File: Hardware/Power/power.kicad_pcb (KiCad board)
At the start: 4 copper layers, 70 x 67.5 mm, 33 parts, among them J1 Conn_02x23_Odd_Even, J2 Screw_Terminal_01x03, J3 Conn_02x23_Odd_Even, Q1 SI2347DS-T1-GE3, T1 10V, T2 VCC, T3 GND, T4 GND, T5 5V, T6 3V3, T7 GND, U1 TPS563200, U2 TPS563300DRLR, U3 LM1117-3.3

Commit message: schematic update & pcb update
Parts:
- removed C17: 22u, Capacitor_SMD:C_0603_1608Metric_Pad1.08x0.95mm_HandSolder
- removed D5: LD3V3, LED_SMD:LED_0603_1608Metric_Pad1.05x0.95mm_HandSolder
- removed J2: Screw_Terminal_01x03, PLC_STM_Power:TBC05031GG
- removed R8, R9: 1k, Resistor_SMD:R_0603_1608Metric_Pad0.98x0.95mm_HandSolder
- removed U3: LM1117-3.3, Package_TO_SOT_SMD:SOT-223-3_TabPin2
- added C1: 10u, Capacitor_SMD:C_0603_1608Metric_Pad1.08x0.95mm_HandSolder, F.Cu at (138.3, 72.5)
- added C10: 10u, Capacitor_SMD:C_0603_1608Metric_Pad1.08x0.95mm_HandSolder, F.Cu at (142.7, 72.5)
- added C11: 10u, Capacitor_SMD:C_0603_1608Metric_Pad1.08x0.95mm_HandSolder, F.Cu at (142.7, 75.0)
- added C14: 100n, Capacitor_SMD:C_0603_1608Metric_Pad1.08x0.95mm_HandSolder, F.Cu at (142.7, 82.5)
- added C2: 10u, Capacitor_SMD:C_0603_1608Metric_Pad1.08x0.95mm_HandSolder, F.Cu at (138.3, 75.0)
- added C5: 100n, Capacitor_SMD:C_0603_1608Metric_Pad1.08x0.95mm_HandSolder, F.Cu at (138.3, 80.0)
- added C8: 22u, Capacitor_SMD:C_0603_1608Metric_Pad1.08x0.95mm_HandSolder, F.Cu at (138.3, 85.0)
- added C9: 22u, Capacitor_SMD:C_0603_1608Metric_Pad1.08x0.95mm_HandSolder, F.Cu at (138.3, 87.5)
- added F2: 6V/1A, Fuse:Fuse_0805_2012Metric_Pad1.15x1.40mm_HandSolder, F.Cu at (168.3, 84.4)
- added J1: POWER, PLC_STM:1725656, F.Cu at (139.2, 100.1)
- added L1: 3u3/4A95, Inductor_SMD:L_TDK_VLS6045EX_VLS6045AF, F.Cu at (166.9, 75.0)
- added PS1: DPUN02N-15, PLC_STM:DPUN02N15, F.Cu at (141.3, 64.4)
- added R2: 56k2, Resistor_SMD:R_0603_1608Metric_Pad0.98x0.95mm_HandSolder, F.Cu at (147.1, 72.5)
- added R20: 10k, Resistor_SMD:R_0603_1608Metric_Pad0.98x0.95mm_HandSolder, F.Cu at (147.1, 80.0)
- added R4: 1k, Resistor_SMD:R_0603_1608Metric_Pad0.98x0.95mm_HandSolder, F.Cu at (147.1, 75.0)
- added T10: GND, TestPoint:TestPoint_Pad_1.0x1.0mm, F.Cu at (153.8, 85.0)
- added T8: 5V, TestPoint:TestPoint_Pad_1.0x1.0mm, F.Cu at (153.8, 78.8)
- added T9: 3V3, TestPoint:TestPoint_Pad_1.0x1.0mm, F.Cu at (153.8, 81.9)
- C15: value 100n -> 22u
- D3: value LD10V -> LD5V
- D4: value LD10V -> LD3V3
- T1: value 10V -> VCC
- T2: value VCC -> 15V
- T4: value GND -> 5V
- T5: value 5V -> GND
- T6: value 3V3 -> +15V
- T7: value GND -> -15V
- U2: value TPS563300DRLR -> LM1117-3.3; footprint Package_TO_SOT_SMD:SOT-583-8 -> Package_TO_SOT_SMD:SOT-223-3_TabPin2
- moved Q1 84.7 mm to (138.8, 91.0)
- moved D3 74.9 mm to (151.4, 87.8)
- moved D4 74.9 mm to (151.4, 90.4)
- moved U1 74.4 mm to (143.9, 91.2)
- moved U2 72.2 mm to (165.2, 65.1)
- moved C4 67.6 mm to (138.3, 77.5)
- moved C7 67.4 mm to (138.3, 82.5)
- moved D2 65.4 mm to (157.9, 91.4)
- moved C12 63.8 mm to (142.7, 77.5)
- moved C13 63.8 mm to (142.7, 80.0)
- moved R1 63.8 mm to (142.7, 87.5)
- moved T6 63.6 mm to (153.8, 72.8)
- moved T7 63.6 mm to (153.8, 75.8)
- moved C15 63.5 mm to (142.7, 85.0)
- moved R5 62.8 mm to (147.1, 77.5)
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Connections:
- D4 pad 2: /power_section/D10V_R1k -> /power_section/D3V3_R1k
- R5 pad 1: Net-(C8-Pad1) -> /power_section/VO_+3.3V
- R5 pad 2: /power_section/D5V_R1k -> /power_section/D3V3_R1k
- T1 pad 1: +10V -> /power_section/RPP_D
- T2 pad 1: /power_section/RPP_D -> +15V
- T4 pad 1: GND -> Net-(C8-Pad1)
- T5 pad 1: +5V -> GND
- T6 pad 1: /power_section/VO_+3.3V -> +15V
- T7 pad 1: GND -> -15V
- U1 pad 3: +10V -> +15V
- U1 pad 5: Net-(U1-EN) -> +15V
- U2 pad 1: unconnected-(U2-NC-Pad1) -> GND
- U2 pad 2: unconnected-(U2-EN-Pad2) -> /power_section/VO_+3.3V
- U2 pad 3: /power_section/VCC_IN -> +5V

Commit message: schematic update & pcb update
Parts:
- removed the J1 at (119.2, 52.5)
- added J2: NUCLEO LEFT, PLC_STM:PRT12790, F.Cu at (119.2, 52.5)
- J3: value Conn_02x23_Odd_Even -> NUCLEO RIGHT; footprint PLC_STM_Power:PRT12790 -> PLC_STM:PRT12790
- moved J3 56.0 mm to (180.2, 52.5), turned to -90 degrees
- moved F3 40.4 mm to (137.5, 61.2), turned to 90 degrees
- moved PS1 40.3 mm to (142.7, 104.8)
- moved D1 36.1 mm to (131.8, 92.0), turned to 90 degrees
- moved C1 34.7 mm to (171.8, 81.8), turned to 90 degrees
- moved C2 32.1 mm to (169.8, 81.8), turned to 90 degrees
- moved C10 32.0 mm to (158.6, 100.2), turned to 180 degrees
- moved F1 31.8 mm to (131.8, 99.8), turned to -90 degrees
- moved T1 30.1 mm to (128.5, 93.0), turned to -90 degrees
- moved C11 27.3 mm to (152.6, 100.4)
- moved C8 26.6 mm to (163.5, 76.3), turned to 90 degrees
- moved C9 25.9 mm to (161.8, 76.3), turned to 90 degrees
- moved C5 25.7 mm to (164.0, 81.8), turned to 90 degrees
- moved D4 25.3 mm to (136.8, 69.8), turned to 180 degrees
- moved U1 24.7 mm to (166.8, 81.8), turned to 90 degrees
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- renumbered R20 to R3
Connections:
- net Net-(C8-Pad1) renamed /power_section/+5V_OUT
- net Net-(U1-SW) renamed /power_section/SW_+5V
- net Net-(U1-VBST) renamed /power_section/VBST_+5V
- net Net-(U1-VFB) renamed /power_section/FB_+5V
- F2 pad 2: +3V3 -> +5V
- J3 pad 1: unconnected-(J3-Pin_1-Pad1) -> UART6_TX
- J3 pad 10: unconnected-(J3-Pin_10-Pad10) -> AO_1
- J3 pad 11: unconnected-(J3-Pin_11-Pad11) -> UART6_TX
- J3 pad 12: unconnected-(J3-Pin_12-Pad12) -> ANALOG_IN6
- J3 pad 13: unconnected-(J3-Pin_13-Pad13) -> CAN2_RX
- J3 pad 14: unconnected-(J3-Pin_14-Pad14) -> ANALOG_IN7
- J3 pad 17: unconnected-(J3-Pin_17-Pad17) -> AO_0
- J3 pad 2: unconnected-(J3-Pin_2-Pad2) -> CAN1_RX
- J3 pad 21: unconnected-(J3-Pin_21-Pad21) -> +15V
- J3 pad 23: unconnected-(J3-Pin_23-Pad23) -> AVDD
- J3 pad 25: unconnected-(J3-Pin_25-Pad25) -> AGND
- J3 pad 27: unconnected-(J3-Pin_27-Pad27) -> GND
- J3 pad 39: unconnected-(J3-Pin_39-Pad39) -> GND
- J3 pad 4: unconnected-(J3-Pin_4-Pad4) -> CAN1_TX
- J3 pad 40: unconnected-(J3-Pin_40-Pad40) -> UART6_TX
- J3 pad 42: unconnected-(J3-Pin_42-Pad42) -> UART6_RX
- J3 pad 44: unconnected-(J3-Pin_44-Pad44) -> UART5_TX
- J3 pad 46: unconnected-(J3-Pin_46-Pad46) -> UART5_RX
- J3 pad 5: unconnected-(J3-Pin_5-Pad5) -> CAN2_TX
- J3 pad 6: unconnected-(J3-Pin_6-Pad6) -> AVDD
- J3 pad 7: unconnected-(J3-Pin_7-Pad7) -> CAN2_RX
- J3 pad 8: unconnected-(J3-Pin_8-Pad8) -> GND
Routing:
- net +15V: track 0.00 -> 75.1 mm
- net +5V: track 0.00 -> 69.8 mm
- net -15V: track 0.00 -> 62.0 mm
- net GND: track 0.00 -> 32.2 mm, vias 0 -> 24
- net /power_section/VCC_IN: track 0.00 -> 22.4 mm
- net +3V3: track 0.00 -> 19.3 mm
- net /power_section/+5V_OUT: track 0.00 -> 8.00 mm
- net +24V: track 0.00 -> 7.11 mm
- net /power_section/VO_+3.3V: track 0.00 -> 5.12 mm
- net /power_section/FB_+5V: track 0.00 -> 4.28 mm
- net /power_section/VBST_+5V: track 0.00 -> 4.07 mm
- net /power_section/D5V_R1k: track 0.00 -> 3.24 mm
- net /power_section/RPP_D: track 0.00 -> 2.62 mm
- net /power_section/D3V3_R1k: track 0.00 -> 1.77 mm
- added copper zone on F.Cu, net +5V
- added copper zone on F.Cu, net /power_section/+5V_OUT
- added copper zone on F.Cu, net /power_section/RPP_D
- added copper zone on F.Cu, net /power_section/RPP_G
- added copper zone on F.Cu, net /power_section/SW_+5V
- added copper zone on F.Cu, net /power_section/VCC_IN
- added copper zone on F.Cu, net /power_section/VO_+3.3V
- added copper zone on B.Cu, net GND
- added copper zone on F.Cu, net GND
- added copper zone on In1.Cu, net GND
- added copper zone on In2.Cu, net GND

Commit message: digital output & power finished
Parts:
- renumbered C12 to C10, C13 to C11, C10 to C12, C11 to C13, T8 to T6, T6 to T7, T7 to T8
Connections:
- C3 pad 1: /power_section/VCC_IN -> +24V
- C4 pad 1: /power_section/VCC_IN -> +24V
- C6 pad 1: /power_section/VCC_IN -> +24V
- C7 pad 1: /power_section/VCC_IN -> +24V
- D2 pad 1: /power_section/VCC_IN -> +24V
- F1 pad 2: +24V -> VCC
- J1 pad 2: +24V -> VCC
- J2 pad 10: UART5_TX -> +15V
- J2 pad 11: GND -> unconnected-(J2-Pin_11-Pad11)
- J2 pad 12: UART5_RX -> unconnected-(J2-Pin_12-Pad12)
- J2 pad 13: GND -> unconnected-(J2-Pin_13-Pad13)
- J2 pad 15: +5V -> unconnected-(J2-Pin_15-Pad15)
- J2 pad 18: -15V -> unconnected-(J2-Pin_18-Pad18)
- J2 pad 19: unconnected-(J2-Pin_19-Pad19) -> GND
- J2 pad 20: unconnected-(J2-Pin_20-Pad20) -> GND
- J2 pad 22: UART2_RX -> GND
- J2 pad 24: UART2_TX -> unconnected-(J2-Pin_24-Pad24)
- J2 pad 25: unconnected-(J2-Pin_25-Pad25) -> +3V3
- J2 pad 26: unconnected-(J2-Pin_26-Pad26) -> -15V
- J2 pad 27: unconnected-(J2-Pin_27-Pad27) -> +5V
- J2 pad 29: unconnected-(J2-Pin_29-Pad29) -> +24V
- J2 pad 30: GND -> unconnected-(J2-Pin_30-Pad30)
- J2 pad 39: GND -> unconnected-(J2-Pin_39-Pad39)
- J2 pad 41: CAN1_RX -> unconnected-(J2-Pin_41-Pad41)
- J2 pad 43: CAN1_TX -> unconnected-(J2-Pin_43-Pad43)
- J2 pad 6: UART4_TX -> unconnected-(J2-Pin_6-Pad6)
- J2 pad 7: +3V3 -> unconnected-(J2-Pin_7-Pad7)
- J2 pad 8: UART4_RX -> unconnected-(J2-Pin_8-Pad8)
- J2 pad 9: +5V -> unconnected-(J2-Pin_9-Pad9)
- J3 pad 1: UART6_TX -> unconnected-(J3-Pin_1-Pad1)
- J3 pad 10: AO_1 -> unconnected-(J3-Pin_10-Pad10)
- J3 pad 11: UART6_TX -> unconnected-(J3-Pin_11-Pad11)
- J3 pad 12: ANALOG_IN6 -> unconnected-(J3-Pin_12-Pad12)
- J3 pad 13: CAN2_RX -> unconnected-(J3-Pin_13-Pad13)
- J3 pad 14: ANALOG_IN7 -> unconnected-(J3-Pin_14-Pad14)
- J3 pad 17: AO_0 -> unconnected-(J3-Pin_17-Pad17)
- J3 pad 2: CAN1_RX -> unconnected-(J3-Pin_2-Pad2)
- J3 pad 20: unconnected-(J3-Pin_20-Pad20) -> GND
- J3 pad 21: +15V -> unconnected-(J3-Pin_21-Pad21)
- J3 pad 23: AVDD -> unconnected-(J3-Pin_23-Pad23)
- J3 pad 25: AGND -> unconnected-(J3-Pin_25-Pad25)
- J3 pad 27: GND -> unconnected-(J3-Pin_27-Pad27)
- J3 pad 4: CAN1_TX -> unconnected-(J3-Pin_4-Pad4)
- J3 pad 40: UART6_TX -> unconnected-(J3-Pin_40-Pad40)
- J3 pad 42: UART6_RX -> unconnected-(J3-Pin_42-Pad42)
- J3 pad 44: UART5_TX -> unconnected-(J3-Pin_44-Pad44)
- J3 pad 46: UART5_RX -> unconnected-(J3-Pin_46-Pad46)
- J3 pad 5: CAN2_TX -> unconnected-(J3-Pin_5-Pad5)
- J3 pad 6: AVDD -> unconnected-(J3-Pin_6-Pad6)
- J3 pad 7: CAN2_RX -> unconnected-(J3-Pin_7-Pad7)
- J3 pad 8: GND -> unconnected-(J3-Pin_8-Pad8)
- PS1 pad 1: /power_section/VCC_IN -> +24V
- Q1 pad 2: /power_section/VCC_IN -> +24V
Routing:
- net +24V: track 7.11 -> 67.0 mm, vias 0 -> 1
- net +15V: track 75.1 -> 112.8 mm, vias 0 -> 1
- net /power_section/VCC_IN: track 22.4 -> 0.00 mm
- net +3V3: track 19.3 -> 39.2 mm, vias 0 -> 1
- net +5V: track 69.8 -> 57.2 mm
- net VCC: track 0.00 -> 7.11 mm
- net -15V: track 62.0 -> 62.6 mm
- added copper zone on F.Cu, net +24V
- removed copper zone on F.Cu, net /power_section/VCC_IN
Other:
- board text removed: "®©®"

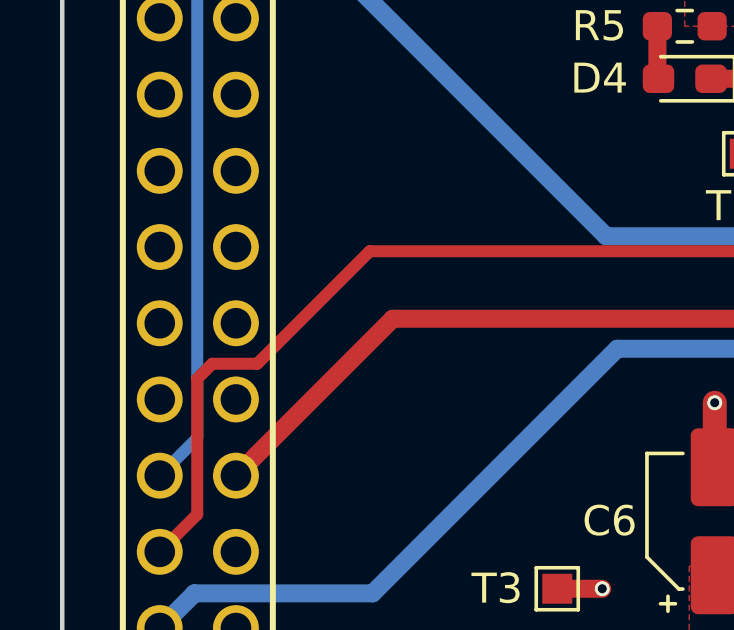
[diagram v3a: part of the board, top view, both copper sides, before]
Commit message: analog & can finished
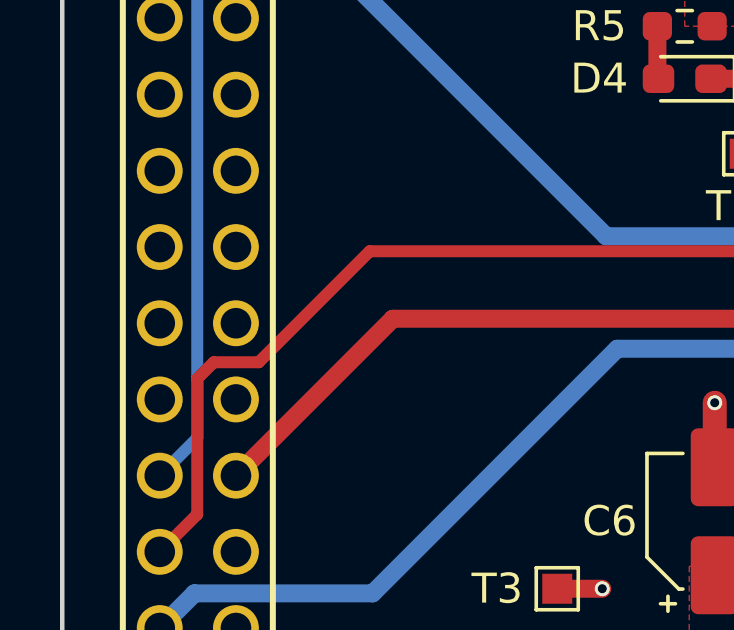
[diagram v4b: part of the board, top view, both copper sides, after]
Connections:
- J3 pad 39: GND -> unconnected-(J3-Pin_39-Pad39)
- J3 pad 9: unconnected-(J3-Pin_9-Pad9) -> GND
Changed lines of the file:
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@@
 	(net 26 "unconnected-(J3-Pin_15-Pad15)")
 	(net 27 "unconnected-(J3-Pin_29-Pad29)")
-	(net 28 "unconnected-(J3-Pin_9-Pad9)")
+	(net 28 "unconnected-(J3-Pin_39-Pad39)")
 	(net 29 "unconnected-(J3-Pin_41-Pad41)")
 	(net 30 "unconnected-(J3-Pin_19-Pad19)")
@@
 			(layers "*.Cu" "*.Mask")
 			(remove_unused_layers no)
-			(net 28 "unconnected-(J3-Pin_9-Pad9)")
+			(net 2 "GND")
 			(pinfunction "Pin_9")
-			(pintype "passive+no_connect")
+			(pintype "passive")
 		)
 		(pad "10" thru_hole circle
@@
 			(layers "*.Cu" "*.Mask")
 			(remove_unused_layers no)
-			(net 2 "GND")
+			(net 28 "unconnected-(J3-Pin_39-Pad39)")
 			(pinfunction "Pin_39")
-			(pintype "passive")
+			(pintype "passive+no_connect")
 		)
 		(pad "40" thru_hole circle
@@
 		(layer "Dwgs.User")
 		(pts
-			(xy 135 48.5) (xy 137 56.5)
-		)
-		(height 6)
-		(orientation 1)
-		(format
-			(prefix "")
-			(suffix "")
-			(units 3)
-			(units_format 1)
-			(precision 4)
-			(suppress_zeroes yes)
-		)
-		(style
-			(thickness 0.1)
-			(arrow_length 1.27)
-			(text_position_mode 1)
-			(arrow_direction outward)
-			(extension_height 0.58642)
-			(extension_offset 0.5)
-			(keep_text_aligned yes)
-		)
-		(gr_text "8 mm"
-			(at 141 52.5 90)
-			(layer "Dwgs.User")
-			(effects
-				(font
-					(size 0.8 0.8)
-					(thickness 0.1)
-				)
-			)
-		)
-	)
-	(dimension
-		(type orthogonal)
-		(layer "Dwgs.User")
-		(pts
 			(xy 116 112) (xy 186 112)
 		)
@@
 		)
 	)
-	(dimension
-		(type orthogonal)
-		(layer "Dwgs.User")
-		(pts
-			(xy 135 48.5) (xy 167 48.5)
-		)
-		(height -2.5)
-		(orientation 0)
-		(format
-			(prefix "")
-			(suffix "")
-			(units 3)
-			(units_format 1)
-			(precision 4)
-			(suppress_zeroes yes)
-		)
-		(style
-			(thickness 0.1)
-			(arrow_length 1.27)
-			(text_position_mode 1)
-			(arrow_direction outward)
-			(extension_height 0.58642)
-			(extension_offset 0.5)
-			(keep_text_aligned yes)
-		)
-		(gr_text "32 mm"
-			(at 151 46 0)
-			(layer "Dwgs.User")
-			(effects
-				(font
-					(size 0.8 0.8)
-					(thickness 0.1)
-				)
-			)
-		)
-	)
 	(segment
 		(start 133.25 109.71)
@@
 	)
 	(segment
-		(start 150.25 66.75)
-		(end 149.1375 65.6375)
-		(width 0.6)
+		(start 120.5 79.75)
+		(end 121.05 79.2)
+		(width 0.4)
 		(layer "F.Cu")
 		(net 3)
 	)
 	(segment
-		(start 119.25 85.52)
-		(end 120.5 84.27)
-		(width 0.4)
+		(start 150.25 66.75)
+		(end 149.1375 65.6375)
+		(width 0.6)
 		(layer "F.Cu")
 		(net 3)
 	)
 	(segment
-		(start 121 79.25)
-		(end 122.5 79.25)
+		(start 126.25 75.5)
+		(end 154.975 75.5)
 		(width 0.4)
 		(layer "F.Cu")
@@
 	)
 	(segment
-		(start 149.1375 65.6375)
-		(end 149.1375 64.25)
-		(width 0.6)
+		(start 120.5 84.27)
+		(end 120.5 79.75)
+		(width 0.4)
 		(layer "F.Cu")
 		(net 3)
 	)
 	(segment
-		(start 120.5 84.27)
-		(end 120.5 79.75)
-		(width 0.4)
+		(start 149.1375 65.6375)
+		(end 149.1375 64.25)
+		(width 0.6)
 		(layer "F.Cu")
 		(net 3)
 	)
 	(segment
-		(start 126.25 75.5)
-		(end 154.975 75.5)
+		(start 119.25 85.52)
+		(end 120.5 84.27)
 		(width 0.4)
 		(layer "F.Cu")
@@
 	)
 	(segment
-		(start 122.5 79.25)
+		(start 122.55 79.2)
 		(end 126.25 75.5)
 		(width 0.4)
@@
 	)
 	(segment
-		(start 120.5 79.75)
-		(end 121 79.25)
+		(start 121.05 79.2)
+		(end 122.55 79.2)
 		(width 0.4)
 		(layer "F.Cu")

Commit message: small adjustments and final revision
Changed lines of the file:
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@@
+		(layer "Dwgs.User")
+		(pts
+			(xy 118.02 51.105) (xy 184.02 51.105)
+		)
+		(height -5.105)
+		(orientation 0)
+		(format
+			(prefix "")
+			(suffix "")
+			(units 3)
+			(units_format 1)
+			(precision 4)
+			(suppress_zeroes yes)
+		)
+		(style
+			(thickness 0.1)
+			(arrow_length 1.27)
+			(text_position_mode 1)
+			(arrow_direction outward)
+			(extension_height 0.58642)
+			(extension_offset 0.5)
+			(keep_text_aligned yes)
+		)
+		(gr_text "66 mm"
+			(at 151.02 46 0)
+			(layer "Dwgs.User")
+			(effects
+				(font
+					(size 0.8 0.8)
+					(thickness 0.1)
+				)
+			)
+		)
+	)
+	(dimension
+		(type orthogonal)
 		(layer "Dwgs.User")
 		(pts
@@
 	)
 	(segment
-		(start 169.75 83.7)
-		(end 169.75 82.7125)
-		(width 0.6)
-		(layer "F.Cu")
-		(net 8)
-	)
-	(segment
 		(start 164.25 87.75)
 		(end 170.5 87.75)
@@
 	)
 	(segment
+		(start 159.4625 97.2625)
+		(end 159 96.8)
+		(width 0.6)
+		(layer "F.Cu")
+		(net 8)
+	)
+	(segment
 		(start 170.5 87.75)
 		(end 171.75 86.5)
@@
 	)
 	(segment
-		(start 158.2 96.8)
-		(end 159.5 95.5)
+		(start 159.4625 100.4)
+		(end 159.4625 97.2625)
 		(width 0.6)
 		(layer "F.Cu")
@@
 	)
 	(segment
-		(start 158.2 96.8)
-		(end 157.2 96.8)
-		(width 0.6)
-		(layer "F.Cu")
-		(net 8)
-	)
-	(segment
-		(start 168 84.45)
-		(end 169 84.45)
-		(width 0.6)
+		(start 169.75 83.85)
+		(end 169.75 82.7125)
+		(width 0.4)
 		(layer "F.Cu")
 		(net 8)
@@
 	)
 	(segment
-		(start 159.4625 98.0625)
-		(end 158.2 96.8)
-		(width 0.6)
-		(layer "F.Cu")
-		(net 8)
-	)
-	(segment
 		(start 161.8125 101.4125)
 		(end 160.65 100.25)
@@
 	)
 	(segment
+		(start 157.2 96.8)
+		(end 159 96.8)
+		(width 0.6)
+		(layer "F.Cu")
+		(net 8)
+	)
+	(segment
+		(start 167.7 84.1)
+		(end 168 84.4)
+		(width 0.4)
+		(layer "F.Cu")
+		(net 8)
+	)
+	(segment
+		(start 168 84.4)
+		(end 169.2 84.4)
+		(width 0.4)
+		(layer "F.Cu")
+		(net 8)
+	)
+	(segment
 		(start 171.75 86.5)
 		(end 171.75 82.7125)
@@
 	)
 	(segment
-		(start 167.7 84.15)
-		(end 168 84.45)
-		(width 0.6)
-		(layer "F.Cu")
-		(net 8)
-	)
-	(segment
-		(start 159.4625 100.4)
-		(end 159.4625 98.0625)
+		(start 167.7 82.9875)
+		(end 167.7 84.1)
+		(width 0.4)
+		(layer "F.Cu")
+		(net 8)
+	)
+	(segment
+		(start 159.5 96.3)
+		(end 159.5 92.5)
 		(width 0.6)
 		(layer "F.Cu")
@@
 	)
 	(segment
-		(start 167.7 82.9875)
-		(end 167.7 84.15)
-		(width 0.6)
-		(layer "F.Cu")
-		(net 8)
-	)
-	(segment
 		(start 161.8125 104.3875)
 		(end 161.8125 101.4125)
@@
 	)
 	(segment
+		(start 169.2 84.4)
+		(end 169.75 83.85)
+		(width 0.4)
+		(layer "F.Cu")
+		(net 8)
+	)
+	(segment
 		(start 174.25 82.7)
 		(end 171.7625 82.7)
@@
 	)
 	(segment
-		(start 159.5 95.5)
-		(end 159.5 92.5)
-		(width 0.6)
-		(layer "F.Cu")
-		(net 8)
-	)
-	(segment
 		(start 160.65 100.25)
 		(end 159.4625 100.25)
@@
 	)
 	(segment
-		(start 169 84.45)
-		(end 169.75 83.7)
+		(start 159 96.8)
+		(end 159.5 96.3)
 		(width 0.6)
 		(layer "F.Cu")
@@
 	)
 	(segment
-		(start 154 79.5)
-		(end 154 87)
-		(width 0.6)
-		(layer "B.Cu")
-		(net 8)
-	)
-	(segment
-		(start 121.79 62.66)
-		(end 134.13 75)
-		(width 0.6)
-		(layer "B.Cu")
-		(net 8)
-	)
-	(segment
-		(start 149.5 75)
-		(end 154 79.5)
-		(width 0.6)
-		(layer "B.Cu")
-		(net 8)
-	)
-	(segment
-		(start 154 87)
-		(end 158 91)
-		(width 0.6)
-		(layer "B.Cu")
-		(net 8)
-	)
-	(segment
-		(start 134.13 75)
-		(end 149.5 75)
+		(start 158 91)
+		(end 154.8 87.8)
+		(width 0.6)
+		(layer "B.Cu")
+		(net 8)
+	)
+	(segment
+		(start 148.6 74)
+		(end 133.13 74)
+		(width 0.6)
+		(layer "B.Cu")
+		(net 8)
+	)
+	(segment
+		(start 154.8 80.2)
+		(end 148.6 74)
+		(width 0.6)
+		(layer "B.Cu")
+		(net 8)
+	)
+	(segment
+		(start 154.8 87.8)
+		(end 154.8 80.2)
+		(width 0.6)
+		(layer "B.Cu")
+		(net 8)
+	)
+	(segment
+		(start 133.13 74)
+		(end 121.79 62.66)
 		(width 0.6)
 		(layer "B.Cu")
@@
 	)
 	(segment
-		(start 133 60.225)
+		(start 134.3 60.225)
 		(end 137.5 60.225)
 		(width 0.4)
@@
 	)
 	(via
-		(at 133 60.225)
-		(size 0.5)
-		(drill 0.3)
-		(layers "F.Cu" "B.Cu")
+		(at 134.3 60.225)
+		(size 0.5)
+		(drill 0.3)
+		(layers "F.Cu" "B.Cu")
+		(net 11)
+	)
+	(segment
+		(start 130.85 61.4)
+		(end 121.12859 61.4)
+		(width 0.4)
+		(layer "B.Cu")
 		(net 11)
 	)
@@
 	)
 	(segment
-		(start 133 60.225)
+		(start 134.3 60.225)
 		(end 132.025 60.225)
 		(width 0.4)
@@
 	)
 	(segment
-		(start 130.85 61.4)
-		(end 121.12859 61.4)
-		(width 0.4)
-		(layer "B.Cu")
-		(net 11)
-	)
-	(segment
-		(start 154.25 86)
+		(start 153.4625 97.7625)
+		(end 153.4625 100.4)
+		(width 0.6)
+		(layer "F.Cu")
+		(net 12)
+	)
+	(segment
+		(start 152.7 97)
+		(end 153.4625 97.7625)
+		(width 0.6)
+		(layer "F.Cu")
+		(net 12)
+	)
+	(segment
+		(start 152.7 97)
+		(end 153.5 96.2)
+		(width 0.6)
+		(layer "F.Cu")
+		(net 12)
+	)
+	(segment
+		(start 153.5 85.25)
 		(end 146 77.75)
 		(width 0.6)
@@
 	)
 	(segment
+		(start 157.95 102.75)
+		(end 155.6 100.4)
+		(width 0.6)
+		(layer "F.Cu")
+		(net 12)
+	)
+	(segment
 		(start 146 77.75)
 		(end 127.02 77.75)
@@
 	)
 	(segment
-		(start 157.95 102.75)
-		(end 155.6 100.4)
-		(width 0.6)
-		(layer "F.Cu")
-		(net 12)
-	)
-	(segment
-		(start 153.4625 100.4)
-		(end 153.4625 98.6625)
-		(width 0.6)
-		(layer "F.Cu")
-		(net 12)
-	)
-	(segment
-		(start 151.8 97)
-		(end 150.8 97)
-		(width 0.6)
-		(layer "F.Cu")
-		(net 12)
-	)
-	(segment
 		(start 157.95 104.75)
 		(end 157.95 102.75)
@@
 	)
 	(segment
-		(start 153.4625 98.6625)
-		(end 151.8 97)
-		(width 0.6)
-		(layer "F.Cu")
-		(net 12)
-	)
-	(segment
-		(start 154.25 94.55)
-		(end 154.25 86)
+		(start 153.5 96.2)
+		(end 153.5 85.25)
 		(width 0.6)
 		(layer "F.Cu")
@@
 	)
 	(segment
-		(start 151.8 97)
-		(end 154.25 94.55)
-		(width 0.6)
-		(layer "F.Cu")
+		(start 150.8 97)
+		(end 152.7 97)
+		(width 0.6)
+		(layer "F.Cu")
